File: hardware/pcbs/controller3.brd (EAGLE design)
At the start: 46 x 16 mm, 46 parts, among them U1 ATMEGA328

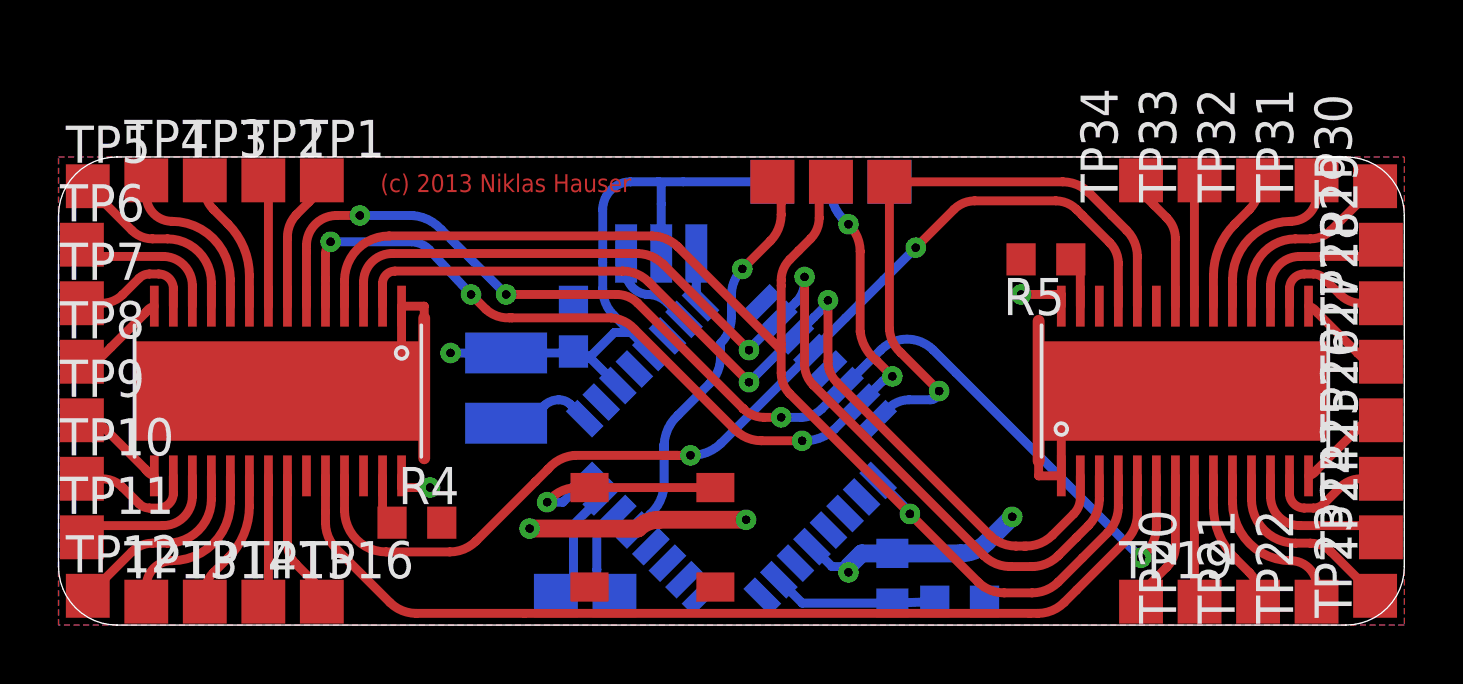
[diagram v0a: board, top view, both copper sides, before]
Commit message: Disconnect thermal pad from GND. Add restrictions for easier soldering.
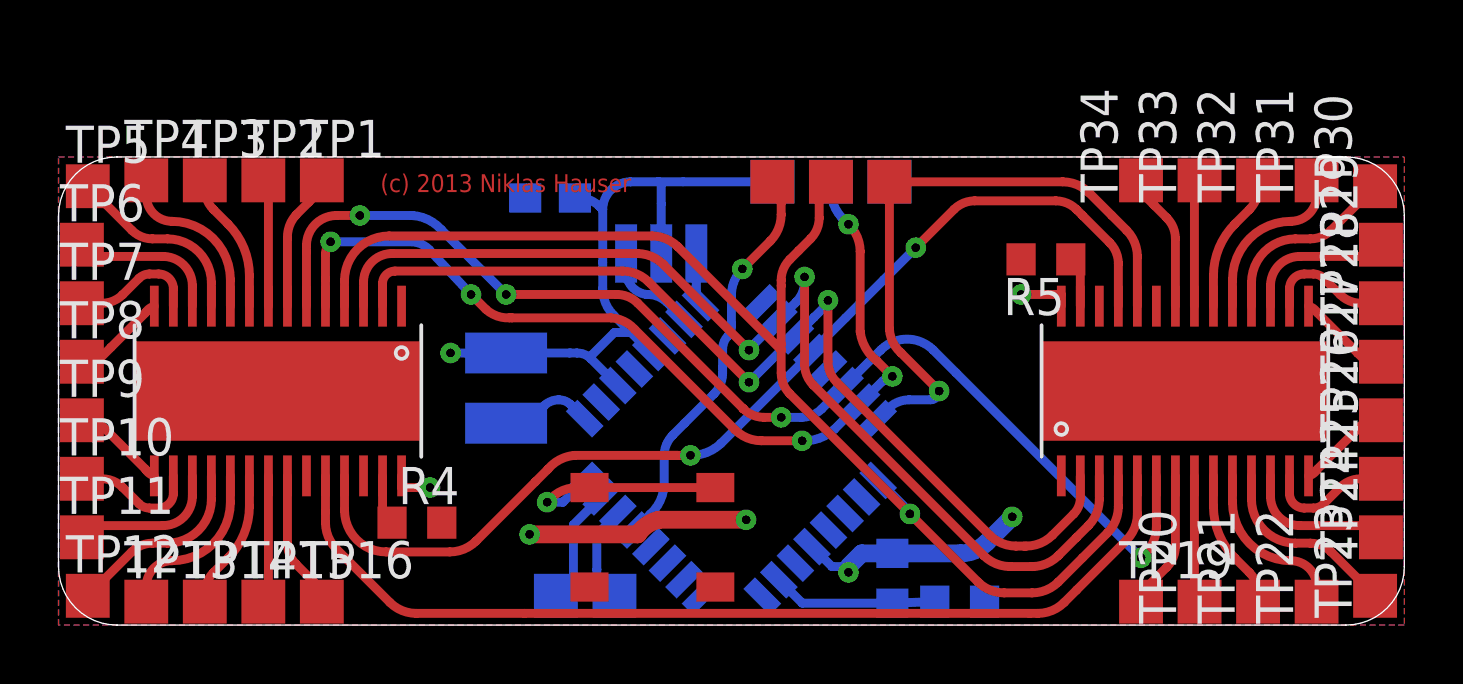
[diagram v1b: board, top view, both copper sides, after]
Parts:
- moved C1 4.47 mm to (16.8, 14.6), turned to 0 degrees
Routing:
- net GND: track 56.4 -> 31.1 mm
- net RESET: track 14.3 -> 13.6 mm
